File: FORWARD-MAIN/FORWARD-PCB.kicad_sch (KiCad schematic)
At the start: 46 parts, among them J1 USB_B_Micro, J2 Conn_01x03_Socket, J5 Conn_01x14_Pin, Q1 SS8050-G, Q2 SS8050-G, U1 BNO055, U2 CP2102N-Axx-xQFN28, U5 ESP32-WROOM-32D

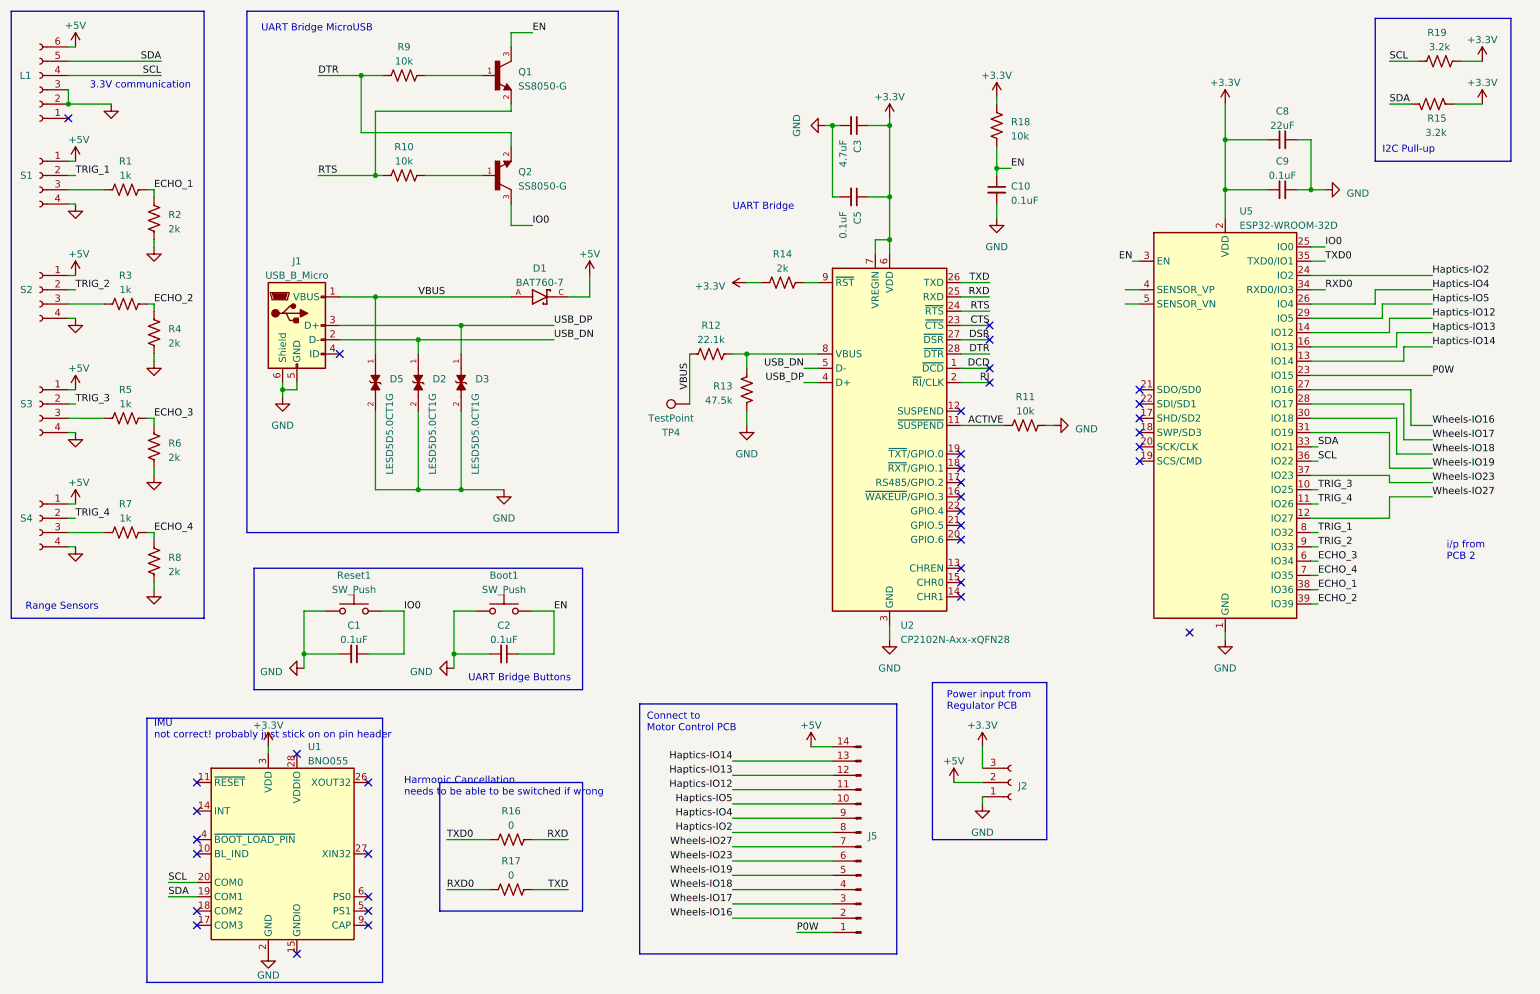
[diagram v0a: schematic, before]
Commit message: autorouting trying but failing
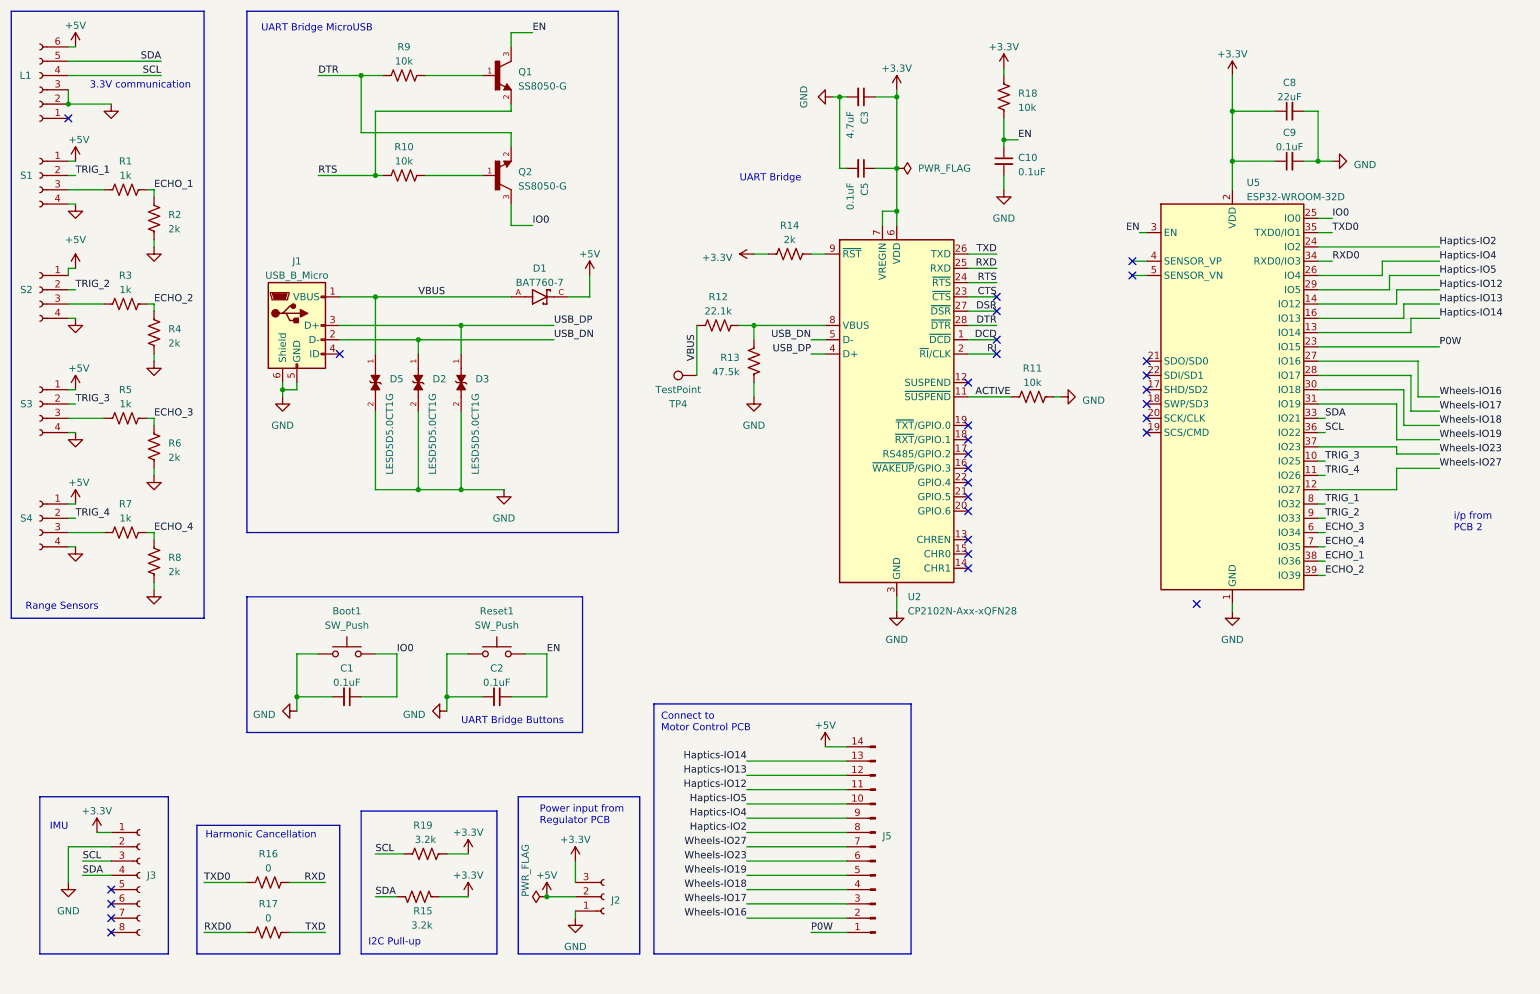
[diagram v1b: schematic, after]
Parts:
- removed U1: BNO055, Package_LGA:LGA-28_5.2x3.8mm_P0.5mm, symbol Sensor_Motion:BNO055
- added J3: Conn_01x08_Socket, Connector_PinSocket_2.54mm:PinSocket_1x08_P2.54mm_Vertical, symbol Connector:Conn_01x08_Socket
- D1: footprint footprints:BAT_2477 -> footprints:SOD2513X120N
- TP4: footprint TestPoint:TestPoint_Loop_D2.50mm_Drill1.0mm_LowProfile -> TestPoint:TestPoint_Pad_1.0x1.0mm
- renumbered Reset1 to Boot1, Boot1 to Reset1
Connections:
- net +3.3V: now also J3.1 (Pin_1)
- net GND: now also J3.2 (Pin_2)
- net SCL: now also J3.3 (Pin_3)
- net SDA: now also J3.4 (Pin_4)
- no-connect marks 37 -> 30
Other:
- note added: "Harmonic Cancellation"
- note added: "IMU"
- note removed: "Harmonic Cancellation needs to be able to be switched if wrong"
- note removed: "IMU not correct! probably just stick on on pin header"
- moved on the sheet: Boot1, C1, C10, C2, C3, C5, C8, C9, J2, J5, R11, R12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

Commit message: routing progress
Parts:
- J5: value Conn_01x14_Pin -> Conn_01x14_Socket; footprint Connector_PinHeader_2.54mm:PinHeader_1x14_P2.54mm_Horizontal -> Connector_Phoenix_MC:PhoenixContact_MC_1,5_14-G-3.81_1x14_P3.81mm_Horizontal
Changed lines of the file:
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@@
 			)
 		)
-		(property "Value" "Conn_01x14_Pin"
+		(property "Value" "Conn_01x14_Socket"
 			(at 168.91 163.195 0)
 			(effects
@@
 			)
 		)
-		(property "Footprint" "Connector_PinHeader_2.54mm:PinHeader_1x14_P2.54mm_Horizontal"
+		(property "Footprint" "Connector_Phoenix_MC:PhoenixContact_MC_1,5_14-G-3.81_1x14_P3.81mm_Horizontal"
 			(at 167.64 162.56 0)
 			(effects
